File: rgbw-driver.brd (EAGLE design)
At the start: 66 x 19.4 mm, 16 parts, among them J1 M20, J2 M20, Q1 STN4NF03L, Q2 STN4NF03L, Q3 STN4NF03L, Q4 STN4NF03L, X1 2PIN

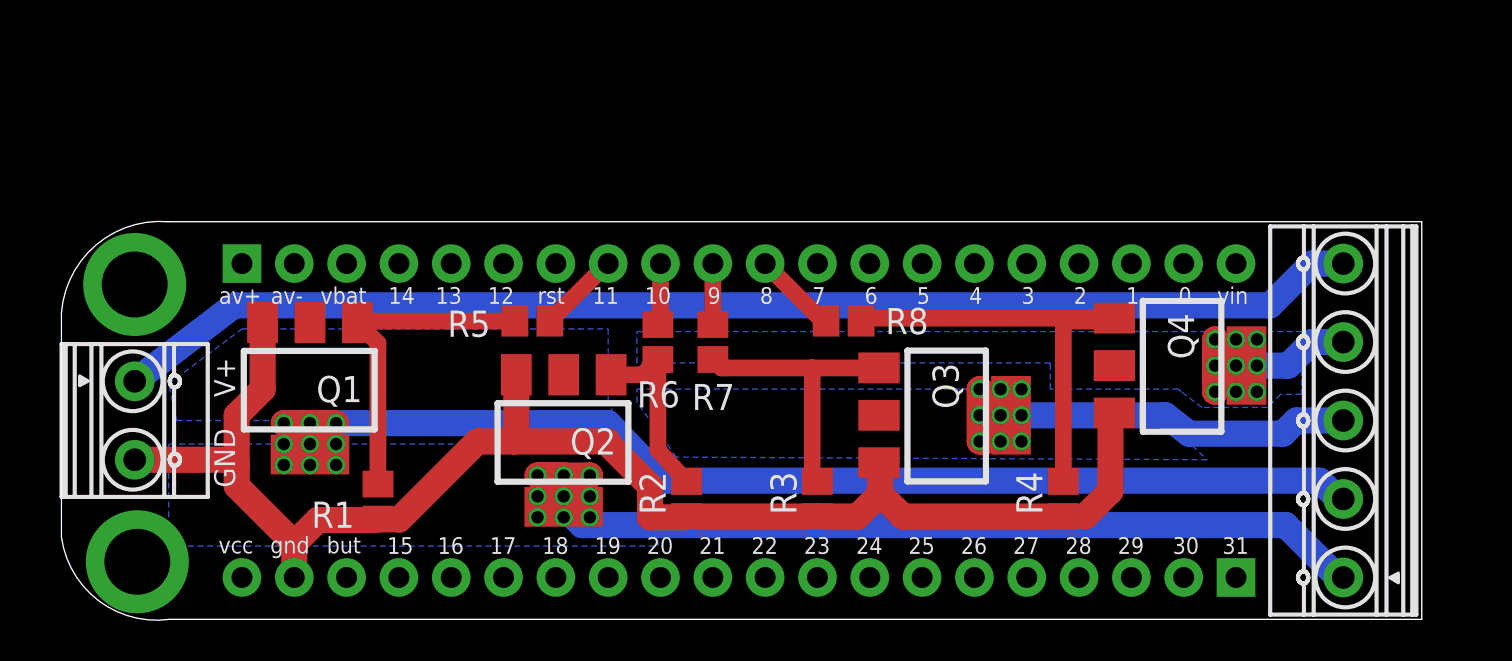
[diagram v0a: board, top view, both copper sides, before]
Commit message: Modifications to allow large heatsink for high current usage
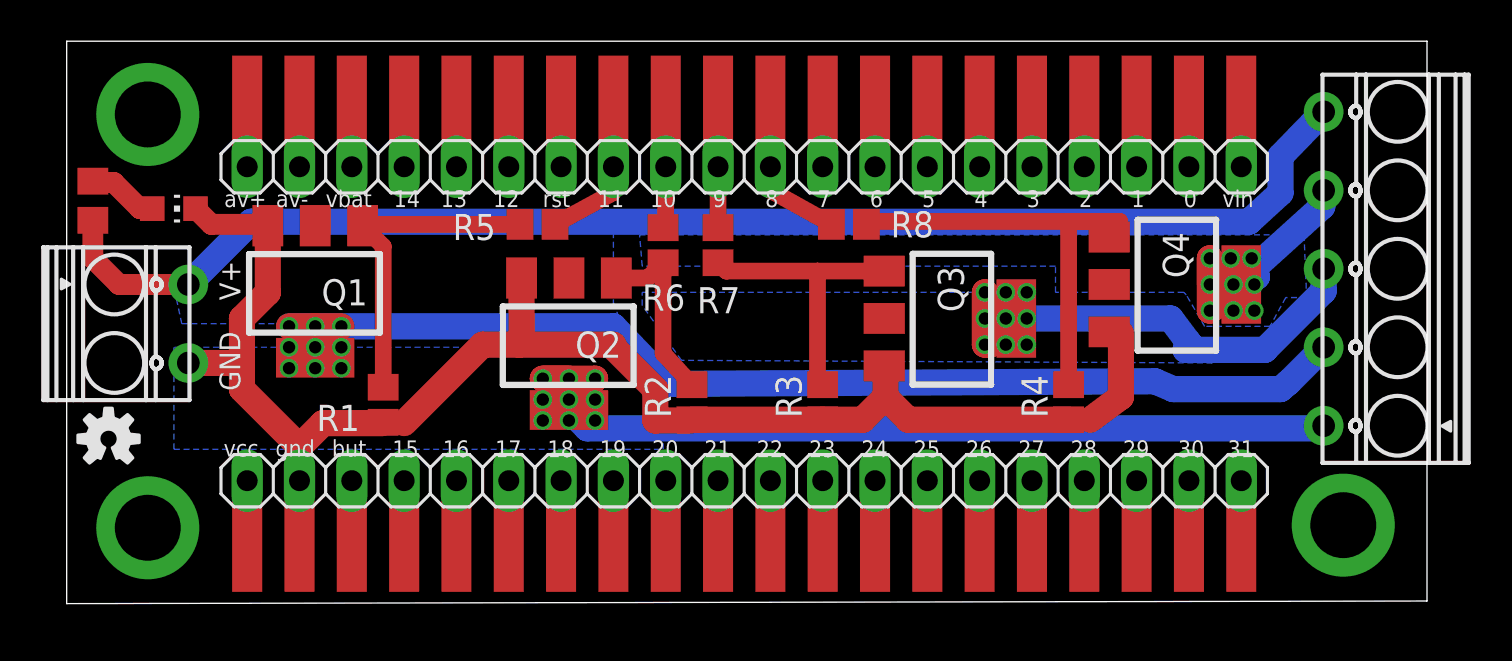
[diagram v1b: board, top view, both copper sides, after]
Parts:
- added LED1: (no value), led:CHIP-LED0805
- added R9: 1K, rcl:R0805
- added U$2: (no value), SparkFun-Aesthetics:OSHW-LOGO-S
- J1, J2: value M20 -> (none); device SparkFun3:1X20 -> header:1X20
- moved J1 24.8 mm to (34.3, 22.1), flipped to the top, turned to 0 degrees
- moved J2 24.3 mm to (34.3, 6.86), flipped to the top, turned to 180 degrees
- moved U$1 7.79 mm to (65.9, 15.2)
- moved X1 4.78 mm to (3.81, 10.7)
- moved R6 4.71 mm to (30.4, 18.3)
- moved R7 4.71 mm to (33.0, 18.3)
- moved R1 4.71 mm to (16.8, 10.5)
- moved R2 4.71 mm to (31.8, 10.7)
- moved R3 4.71 mm to (38.1, 10.7)
- moved Q2 4.71 mm to (25.8, 13.5)
- moved Q3 4.71 mm to (44.3, 14.7)
- moved R5 4.71 mm to (24.3, 19.3)
- moved R4 4.71 mm to (50.0, 10.7)
- moved Q1 4.71 mm to (13.5, 16.0)
- moved R8 4.71 mm to (39.4, 19.3)
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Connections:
- removed net V+: U$1.5, X1.1
- new net N$3: LED1.A, R9.1
- new net N$6: R9.2, U$1.5, X1.1
- net N$4: now also LED1.C
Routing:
- net N$6: track 0.00 -> 66.6 mm
- net V+: track 60.8 -> 0.00 mm
- net N$3: track 0.00 -> 3.44 mm
- net W: track 46.6 -> 44.4 mm
- net R: track 23.5 -> 25.5 mm
- net G: track 11.2 -> 13.1 mm
- net N$5: track 22.7 -> 24.4 mm
- net N$4: track 73.6 -> 75.0 mm
- net B: track 57.1 -> 56.4 mm
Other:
- board size 66 x 19.4 mm -> 66 x 27.3 mm
